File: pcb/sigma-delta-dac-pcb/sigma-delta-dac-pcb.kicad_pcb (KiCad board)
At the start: 2 copper layers, 60 x 32.5 mm, 27 parts, among them J1 Conn_02x03_Top_Bottom, J2 AudioJack3_SwitchTR, U2 TLV9062

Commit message: 아트웍 wip
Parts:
- added C13: 1 nF, Capacitor_SMD:C_0603_1608Metric, F.Cu at (120.0, 102.3)
- added C14: 2.2nF, Capacitor_SMD:C_0603_1608Metric, F.Cu at (126.8, 104.2)
- added C15: 1 nF, Capacitor_SMD:C_0603_1608Metric, F.Cu at (129.6, 109.0)
- added C16: 100nF, Capacitor_SMD:C_0402_1005Metric, F.Cu at (129.8, 96.3)
- added C17: 100nF, Capacitor_SMD:C_0402_1005Metric, F.Cu at (123.2, 103.4)
- added D1: ESD9B5.0ST5G, Diode_SMD:D_SOD-923, F.Cu at (92.8, 95.5)
- added FB2: FerriteBead, Inductor_SMD:L_0805_2012Metric, F.Cu at (106.2, 109.8)
- added R11: 2.61k, Resistor_SMD:R_0603_1608Metric, F.Cu at (118.6, 98.8)
- added R12: 4.87k, Resistor_SMD:R_0603_1608Metric, F.Cu at (120.0, 100.8)
- added R13: 0, Resistor_SMD:R_0805_2012Metric, F.Cu at (134.5, 94.7)
- added R14: 2.61k, Resistor_SMD:R_0603_1608Metric, F.Cu at (125.9, 106.7)
- added R15: 4.87k, Resistor_SMD:R_0603_1608Metric, F.Cu at (128.9, 106.7)
- added R16: 0, Resistor_SMD:R_0805_2012Metric, F.Cu at (134.5, 102.5)
- added R3: 187 k, Resistor_SMD:R_0603_1608Metric, F.Cu at (102.7, 90.8)
- added U1: LM27762, Package_SON:WSON-12-1EP_3x2mm_P0.5mm_EP1x2.65_ThermalVias, F.Cu at (101.8, 94.8)
- added U3: SN74LVC1G125DBV, Package_TO_SOT_SMD:SOT-23-5, F.Cu at (102.1, 112.2)
- added U4: OPA1688IDR, Package_SO:SOIC-8_3.9x4.9mm_P1.27mm, F.Cu at (127.1, 100.0)
- C1, C3: value 100nF -> 4.7 uF; footprint Capacitor_SMD:C_0805_2012Metric_Pad1.18x1.45mm_HandSolder -> Capacitor_SMD:C_0603_1608Metric
- C10: value 100uF -> 470nF; footprint Capacitor_SMD:CP_Elec_6.3x5.3 -> Capacitor_SMD:C_1206_3216Metric
- C11, C8: value 22nF -> 2.2nF; footprint Capacitor_SMD:C_0805_2012Metric_Pad1.18x1.45mm_HandSolder -> Capacitor_SMD:C_0603_1608Metric
- C12: footprint Capacitor_SMD:C_0805_2012Metric_Pad1.18x1.45mm_HandSolder -> Capacitor_SMD:C_0603_1608Metric
- C2: value 100uF -> 1uF; footprint Capacitor_Tantalum_SMD:CP_EIA-3528-15_AVX-H_HandSolder -> Capacitor_SMD:C_0402_1005Metric
- C4: value 100uF -> 2.2uF; footprint Capacitor_Tantalum_SMD:CP_EIA-3528-15_AVX-H_HandSolder -> Capacitor_SMD:C_0402_1005Metric
- C5: value 100uF -> 2.2uF; footprint Capacitor_SMD:CP_Elec_6.3x5.3 -> Capacitor_SMD:C_0402_1005Metric
- C6: footprint Capacitor_SMD:C_0805_2012Metric_Pad1.18x1.45mm_HandSolder -> Capacitor_SMD:C_0402_1005Metric
- C7: value 100nF -> 470nF; footprint Capacitor_SMD:C_0805_2012Metric_Pad1.18x1.45mm_HandSolder -> Capacitor_SMD:C_1206_3216Metric
- C9: value 2.2nF -> 100nF; footprint Capacitor_SMD:C_0805_2012Metric_Pad1.18x1.45mm_HandSolder -> Capacitor_SMD:C_0402_1005Metric
- FB1: value ~ -> FerriteBead; footprint Inductor_SMD:L_0805_2012Metric_Pad1.05x1.20mm_HandSolder -> Inductor_SMD:L_0805_2012Metric
- J1: value Conn_02x03_Top_Bottom -> AudioJack3_SwitchTR; footprint Connector_PinSocket_2.54mm:PinSocket_2x03_P2.54mm_Vertical -> Connector_Audio:Jack_3.5mm_CUI_SJ1-3525N_Horizontal; moved to F.Cu
- J2: value AudioJack3_SwitchTR -> Conn_02x03_Top_Bottom; footprint Connector_Audio:Jack_3.5mm_CUI_SJ1-3525N_Horizontal -> Connector_PinSocket_2.54mm:PinSocket_2x03_P2.54mm_Vertical; moved to B.Cu
- R1, R2: value 0 -> 330; footprint Resistor_SMD:R_0805_2012Metric_Pad1.20x1.40mm_HandSolder -> Resistor_SMD:R_0603_1608Metric
- R10: value 50 -> 100k; footprint Resistor_SMD:R_0805_2012Metric_Pad1.20x1.40mm_HandSolder -> Resistor_SMD:R_0603_1608Metric
- R4: value 0 -> 107 k; footprint Resistor_SMD:R_0805_2012Metric_Pad1.20x1.40mm_HandSolder -> Resistor_SMD:R_0603_1608Metric
- R5: value 220 -> 107 k; footprint Resistor_SMD:R_0805_2012Metric_Pad1.20x1.40mm_HandSolder -> Resistor_SMD:R_0603_1608Metric
- R6: value 2.2k -> 182 k; footprint Resistor_SMD:R_0805_2012Metric_Pad1.20x1.40mm_HandSolder -> Resistor_SMD:R_0603_1608Metric
- R7: value 50 -> 330; footprint Resistor_SMD:R_0805_2012Metric_Pad1.20x1.40mm_HandSolder -> Resistor_SMD:R_0603_1608Metric
- R8: value 220 -> 100k; footprint Resistor_SMD:R_0805_2012Metric_Pad1.20x1.40mm_HandSolder -> Resistor_SMD:R_0603_1608Metric
- R9: value 2.2k -> 330; footprint Resistor_SMD:R_0805_2012Metric_Pad1.20x1.40mm_HandSolder -> Resistor_SMD:R_0603_1608Metric
- U2: value TLV9062 -> SN74LVC1G125DBV; footprint Package_SO:SOIC-8_3.9x4.9mm_P1.27mm -> Package_TO_SOT_SMD:SOT-23-5
- moved J2 53.1 mm to (92.0, 99.7), turned to 180 degrees
- moved J1 51.6 mm to (145.0, 103.0), turned to 90 degrees
- moved C5 32.4 mm to (101.4, 97.1)
- moved C10 22.7 mm to (110.2, 112.8)
- moved C6 19.0 mm to (105.0, 101.2), turned to 90 degrees
- moved U2 16.0 mm to (102.4, 102.7)
- moved C12 15.2 mm to (121.8, 98.8), turned to 0 degrees
- moved R10 15.1 mm to (112.0, 115.5)
- moved C7 14.9 mm to (110.0, 105.0)
- moved FB1 13.8 mm to (107.5, 101.5), turned to 180 degrees
- moved R7 13.6 mm to (104.5, 105.2), turned to 0 degrees
- moved C9 13.1 mm to (103.8, 109.5)
- moved R4 11.4 mm to (100.6, 90.8), turned to -90 degrees
- moved C2 9.09 mm to (104.0, 94.8), turned to -90 degrees
- moved C3 8.49 mm to (98.6, 97.0), turned to 180 degrees
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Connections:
- C10 pad 2: A_OUT_R -> BUFFER_R
- C11 pad 1: Net-(C11-Pad1) -> Net-(C10-Pad1)
- C12 pad 1: Net-(U2B-+) -> Net-(C12-Pad1)
- C12 pad 2: GND -> Net-(U4A--)
- C2 pad 1: 5V_IN -> C+
- C2 pad 2: GND -> C-
- C3 pad 1: Net-(C3-Pad1) -> CP
- C4 pad 1: Net-(C3-Pad1) -> +3V3
- C5 pad 1: Net-(C5-Pad1) -> -3V3
- C5 pad 2: A_OUT_L -> GND
- C6 pad 1: +5V -> Net-(U2-VCC)
- C7 pad 1: +5V -> Net-(C7-Pad1)
- C7 pad 2: GND -> BUFFER_L
- C8 pad 1: Net-(C8-Pad1) -> Net-(C7-Pad1)
- C9 pad 1: Net-(U2A-+) -> Net-(U3-VCC)
- FB1 pad 1: 5V_IN -> +3V3
- FB1 pad 2: Net-(C3-Pad1) -> Net-(U2-VCC)
- R10 pad 1: Net-(U2B--) -> BUFFER_R
- R10 pad 2: Net-(C10-Pad1) -> GND
- R4 pad 1: +5V -> FB+
- R4 pad 2: Net-(C3-Pad1) -> GND
- R5 pad 1: SDM_L -> GND
- R5 pad 2: Net-(C8-Pad1) -> FB-
- R6 pad 1: Net-(C8-Pad1) -> FB-
- R6 pad 2: Net-(U2A-+) -> -3V3
- R7 pad 1: Net-(U2A--) -> Net-(R7-Pad1)
- R7 pad 2: Net-(C5-Pad1) -> Net-(C7-Pad1)
- R8 pad 1: SDM_R -> BUFFER_L
- R8 pad 2: Net-(C11-Pad1) -> GND
- R9 pad 1: Net-(C11-Pad1) -> Net-(R9-Pad1)
- R9 pad 2: Net-(U2B-+) -> Net-(C10-Pad1)
- U2 pad 1: Net-(U2A--) -> GND
- U2 pad 2: Net-(U2A--) -> SDM_L
- U2 pad 3: Net-(U2A-+) -> GND
- U2 pad 4: GND -> Net-(R7-Pad1)
- U2 pad 5: Net-(U2B-+) -> Net-(U2-VCC)
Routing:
- net -3V3: track 0.00 -> 35.3 mm, vias 0 -> 3
- net +5V: track 21.8 -> 0.00 mm
- net Net-(C5-Pad1): track 18.5 -> 0.00 mm, vias 2 -> 0
- net BUFFER_R: track 0.00 -> 15.8 mm
- net Net-(U4A--): track 0.00 -> 15.4 mm
- net +3V3: track 0.00 -> 14.0 mm, vias 0 -> 5
- net 5V_IN: track 15.2 -> 29.0 mm, vias 0 -> 4
- net Net-(U2B-+): track 12.9 -> 0.00 mm
- net Net-(U4B--): track 0.00 -> 11.8 mm
- net Net-(C3-Pad1): track 11.6 -> 0.00 mm
- net BUFFER_L: track 0.00 -> 11.5 mm
- net Net-(U2A-+): track 8.76 -> 0.00 mm
- net FB+: track 0.00 -> 8.39 mm
- net Net-(U4B-+): track 0.00 -> 7.53 mm
- net Net-(U4A-+): track 0.00 -> 5.62 mm
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- added copper zone on In2.Cu, net +3V3
- added copper zone on In1.Cu, net GND
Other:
- copper layers 2 -> 4
- board text removed: "Sigma-Delta-V2"

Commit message: 아트웍 완성 (아마도)
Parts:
- moved R3 1.13 mm to (103.5, 90.0), turned to 180 degrees
- moved C13 1.07 mm to (119.5, 103.2), turned to 90 degrees
- moved R12 0.75 mm to (120.8, 100.8)
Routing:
- net +3V3: track 14.0 -> 17.6 mm, vias 5 -> 10
- net GND: track 14.1 -> 16.8 mm, vias 5 -> 47
- net BUFFER_R: track 15.8 -> 17.9 mm
- net Net-(U4A-+): track 5.62 -> 7.46 mm
- added copper zone on F.Cu, net +3V3
- added copper zone on F.Cu, net -3V3
- added copper zone on In2.Cu, net -3V3

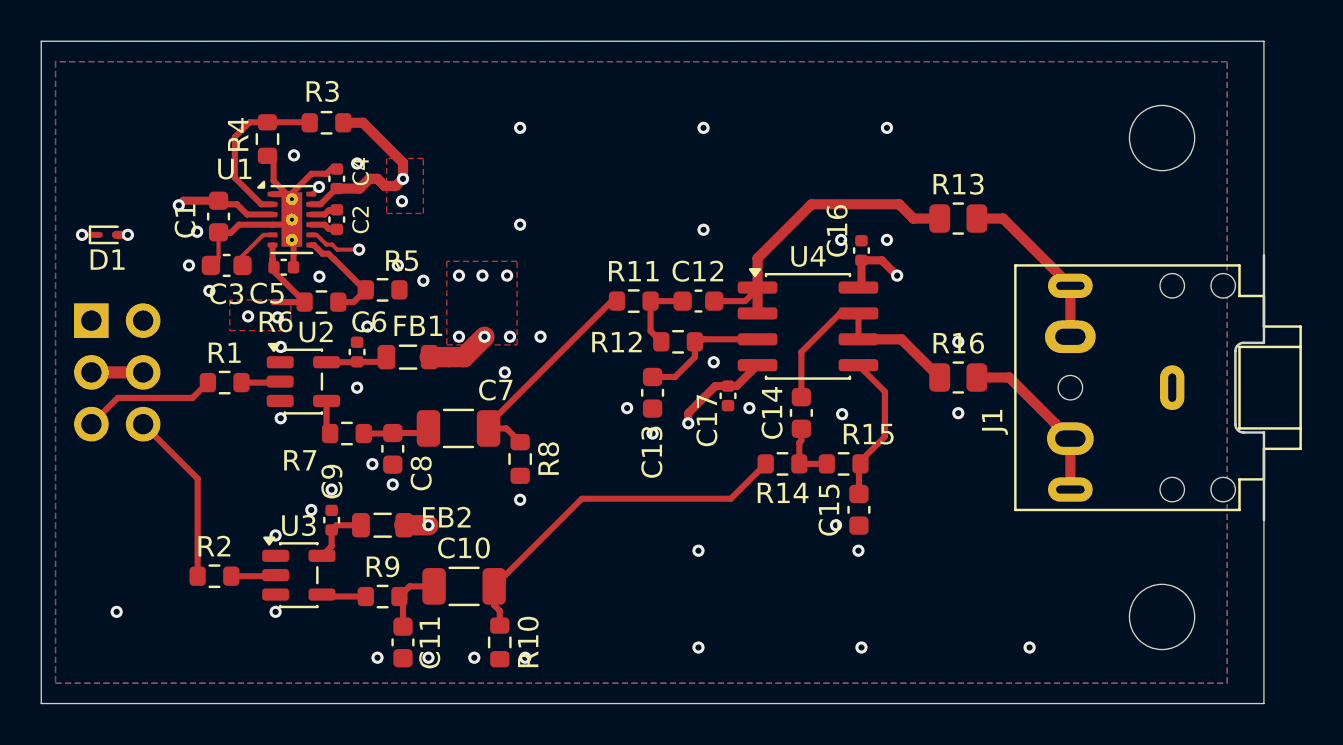
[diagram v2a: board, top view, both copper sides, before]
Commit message: 레이아웃 최적화, opamp 캐패시터 추가
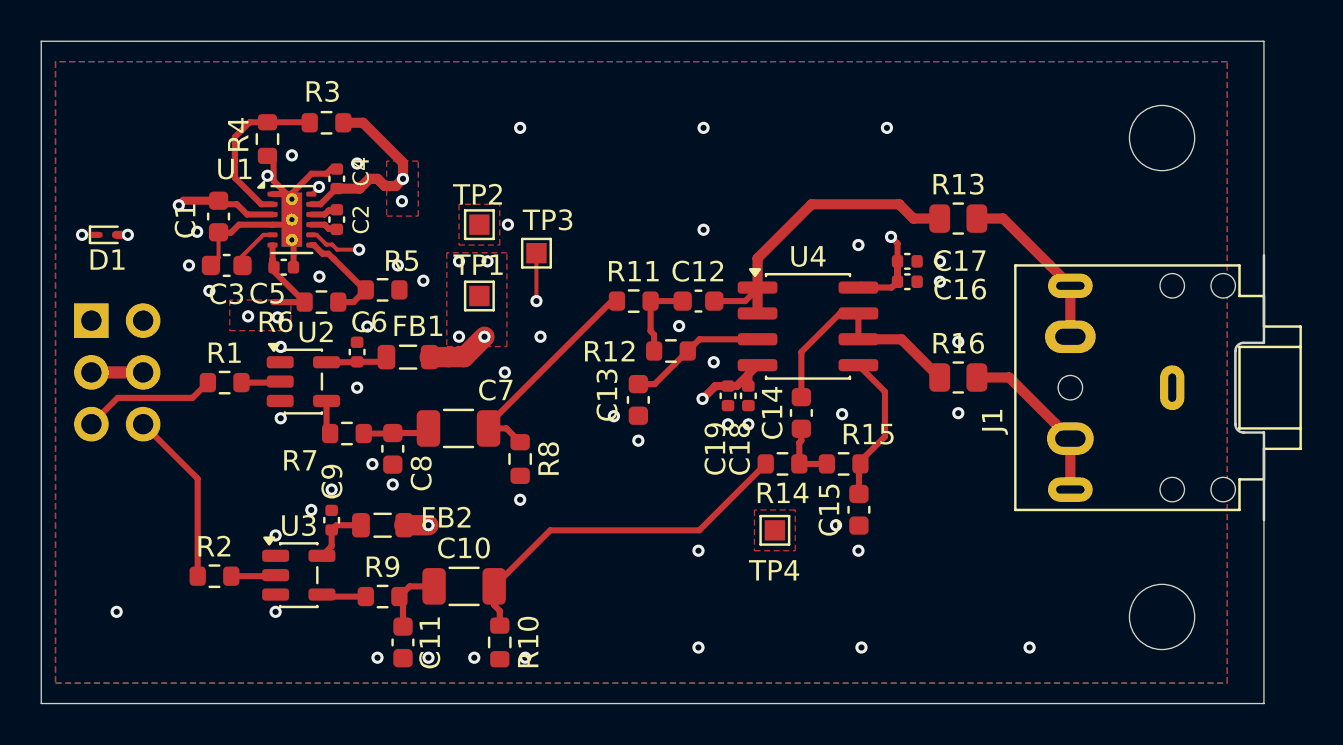
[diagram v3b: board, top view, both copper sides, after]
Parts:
- added C16: 100nF, Capacitor_SMD:C_0402_1005Metric, F.Cu at (132.0, 97.8)
- added C18: 100nF, Capacitor_SMD:C_0402_1005Metric, F.Cu at (124.2, 103.4)
- added TP1: TestPoint, TestPoint:TestPoint_Pad_1.0x1.0mm, F.Cu at (111.0, 98.5)
- added TP2: TestPoint, TestPoint:TestPoint_Pad_1.0x1.0mm, F.Cu at (111.0, 95.0)
- added TP3: TestPoint, TestPoint:TestPoint_Pad_1.0x1.0mm, F.Cu at (113.8, 96.4)
- added TP4: TestPoint, TestPoint:TestPoint_Pad_1.0x1.0mm, F.Cu at (125.5, 110.0)
- moved C17 2.31 mm to (132.0, 96.8), turned to 0 degrees
- moved C13 0.78 mm to (118.8, 103.6)
- moved R12 0.57 mm to (120.4, 101.2)
- renumbered C16 to C17, C17 to C19
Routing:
- net +3V3: track 17.6 -> 19.8 mm, vias 10 -> 8
- net 5V_IN: track 29.3 -> 28.6 mm
- net Net-(U4A-+): track 7.46 -> 6.94 mm
- net -3V3: track 35.4 -> 35.8 mm, vias 3 -> 4
- net GND: vias 47 -> 51

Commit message: via size 수정
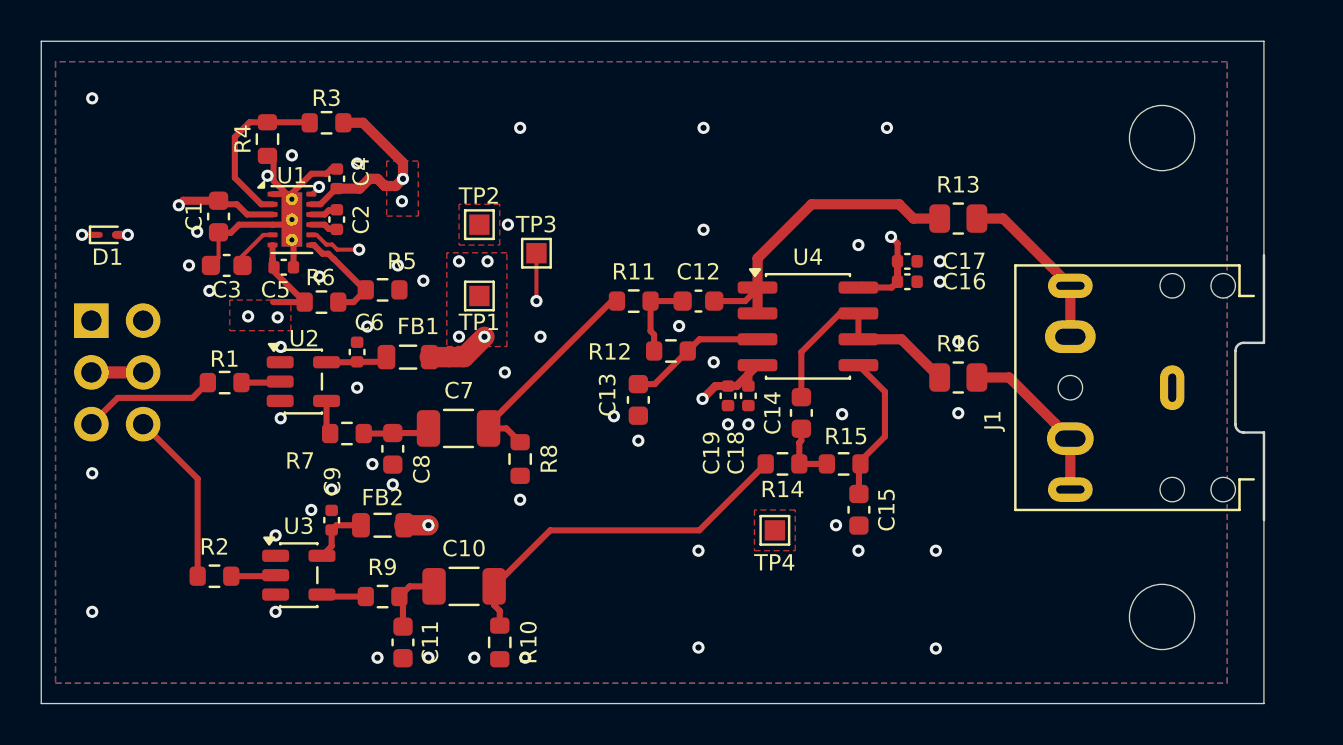
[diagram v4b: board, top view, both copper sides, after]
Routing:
- net GND: vias 51 -> 53
